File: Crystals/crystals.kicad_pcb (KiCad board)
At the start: 2 copper layers, 5 parts

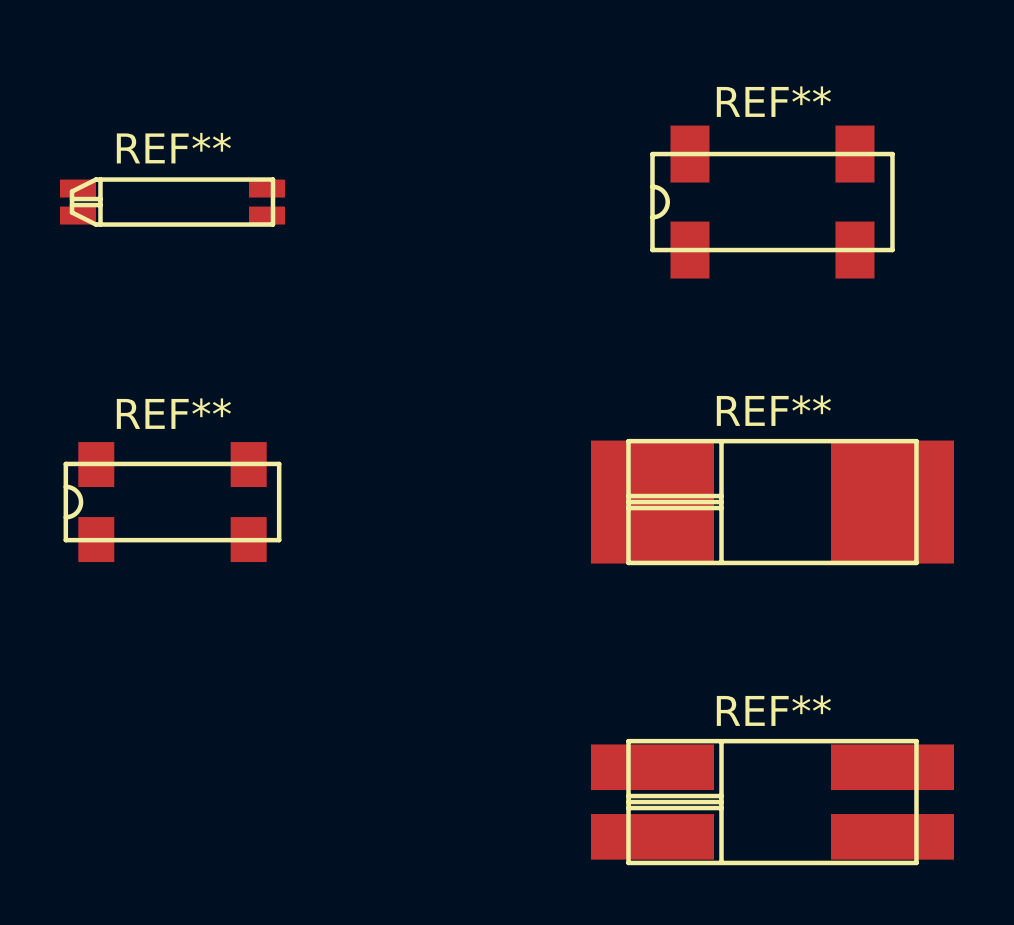
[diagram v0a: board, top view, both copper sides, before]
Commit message: Modified Crystals according to SC's comments on pull request: * Added the Crystal_ prefix to all component names * Clearance increased which is 0.5mm for crystals, according to KLC * Component outline moved to F.Fab, VAL** moved out of the component area * Added simplified outline which does not cover pads to F.Silk
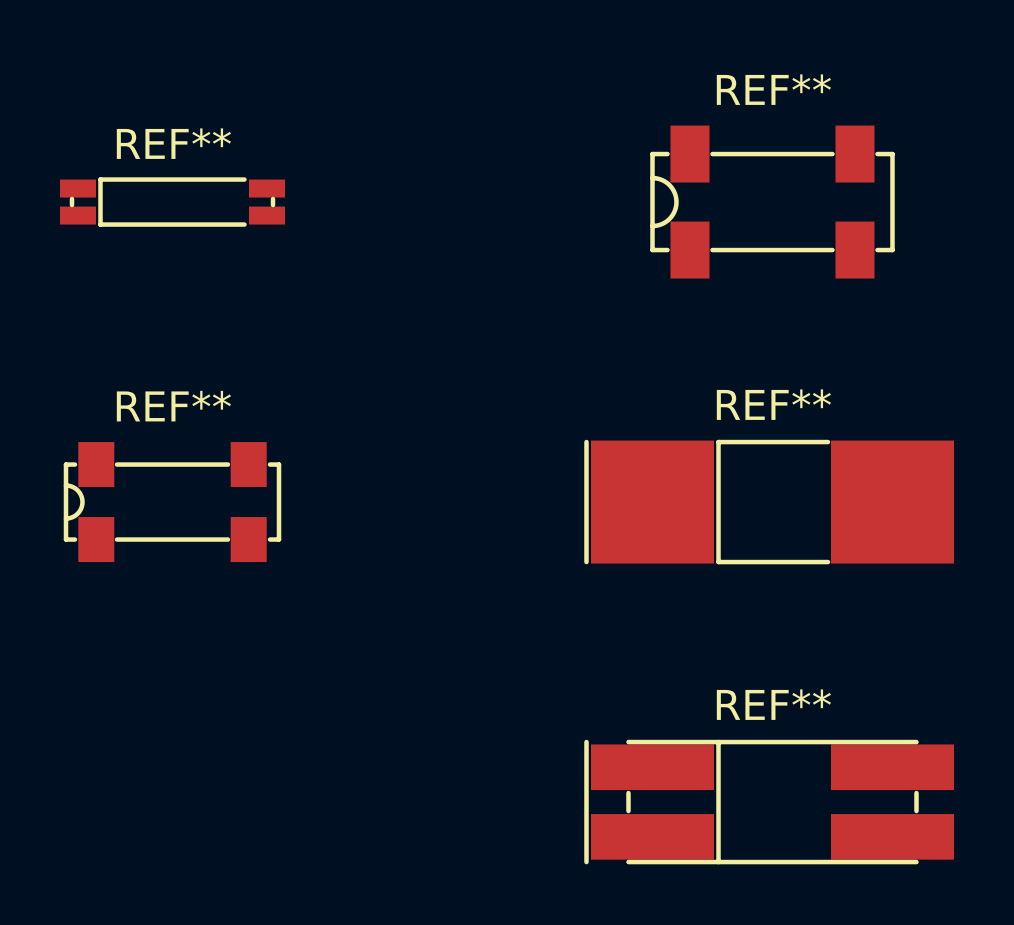
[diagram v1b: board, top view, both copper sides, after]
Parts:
- REF**: value MC-146 -> Crystal_MC-146; footprint Crystals:MC-146 -> Crystals:Crystal_MC-146
- REF**: value MC-156 -> Crystal_MC-156; footprint Crystals:MC-156 -> Crystals:Crystal_MC-156
- REF**: value MC-306 -> Crystal_MC-306; footprint Crystals:MC-306 -> Crystals:Crystal_MC-306
- REF**: value MC-405 -> Crystal_MC-405; footprint Crystals:MC-405 -> Crystals:Crystal_MC-405
- REF**: value MC-406 -> Crystal_MC-406; footprint Crystals:MC-406 -> Crystals:Crystal_MC-406
